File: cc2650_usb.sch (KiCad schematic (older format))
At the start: 29 parts, among them P1 CONN_01X07, P2 CONN_01X04, P3 CONN_01X02, U1 CC2650F128RHB, X1 24Mhz, Y1 32.768kHz

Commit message: Some layout work done
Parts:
- added P4: CONN_01X08, Pin_Headers:Pin_Header_Straight_1x08, symbol CONN_01X08
- ANT1: footprint (none) -> jyd:TI_DN007_2.4GHz
- C1, C10, C11, C12, C13, C14, C15, C16, C17, C2, C3, C4, C5, C6, C7, C8, C9, L1, L2, L3: footprint (none) -> Capacitors_SMD:C_0603
- P1: footprint (none) -> Pin_Headers:Pin_Header_Straight_1x07
- P2: footprint (none) -> Pin_Headers:Pin_Header_Straight_1x04
- P3: footprint (none) -> Pin_Headers:Pin_Header_Straight_1x02
- R1, R2: footprint (none) -> Resistors_SMD:R_0603
- U1: footprint (none) -> Housings_DFN_QFN:QFN-32-1EP_5x5mm_Pitch0.5mm
- X1: footprint (none) -> Crystals:crystal_FA238-TSX3225
- Y1: footprint (none) -> crystals_extra:XTAL3215
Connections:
- net labels added: DIO_10, DIO_11, DIO_12, DIO_13, DIO_14, DIO_7, DIO_8, DIO_9, RF_N, RF_P, X24M_N, X24M_P, X32K_Q1, X32K_Q2
- wire segments 97 -> 136
- no-connect marks 1 -> 4
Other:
- moved on the sheet: ANT1, C14, C15, C16, C17, L2, L3, R2

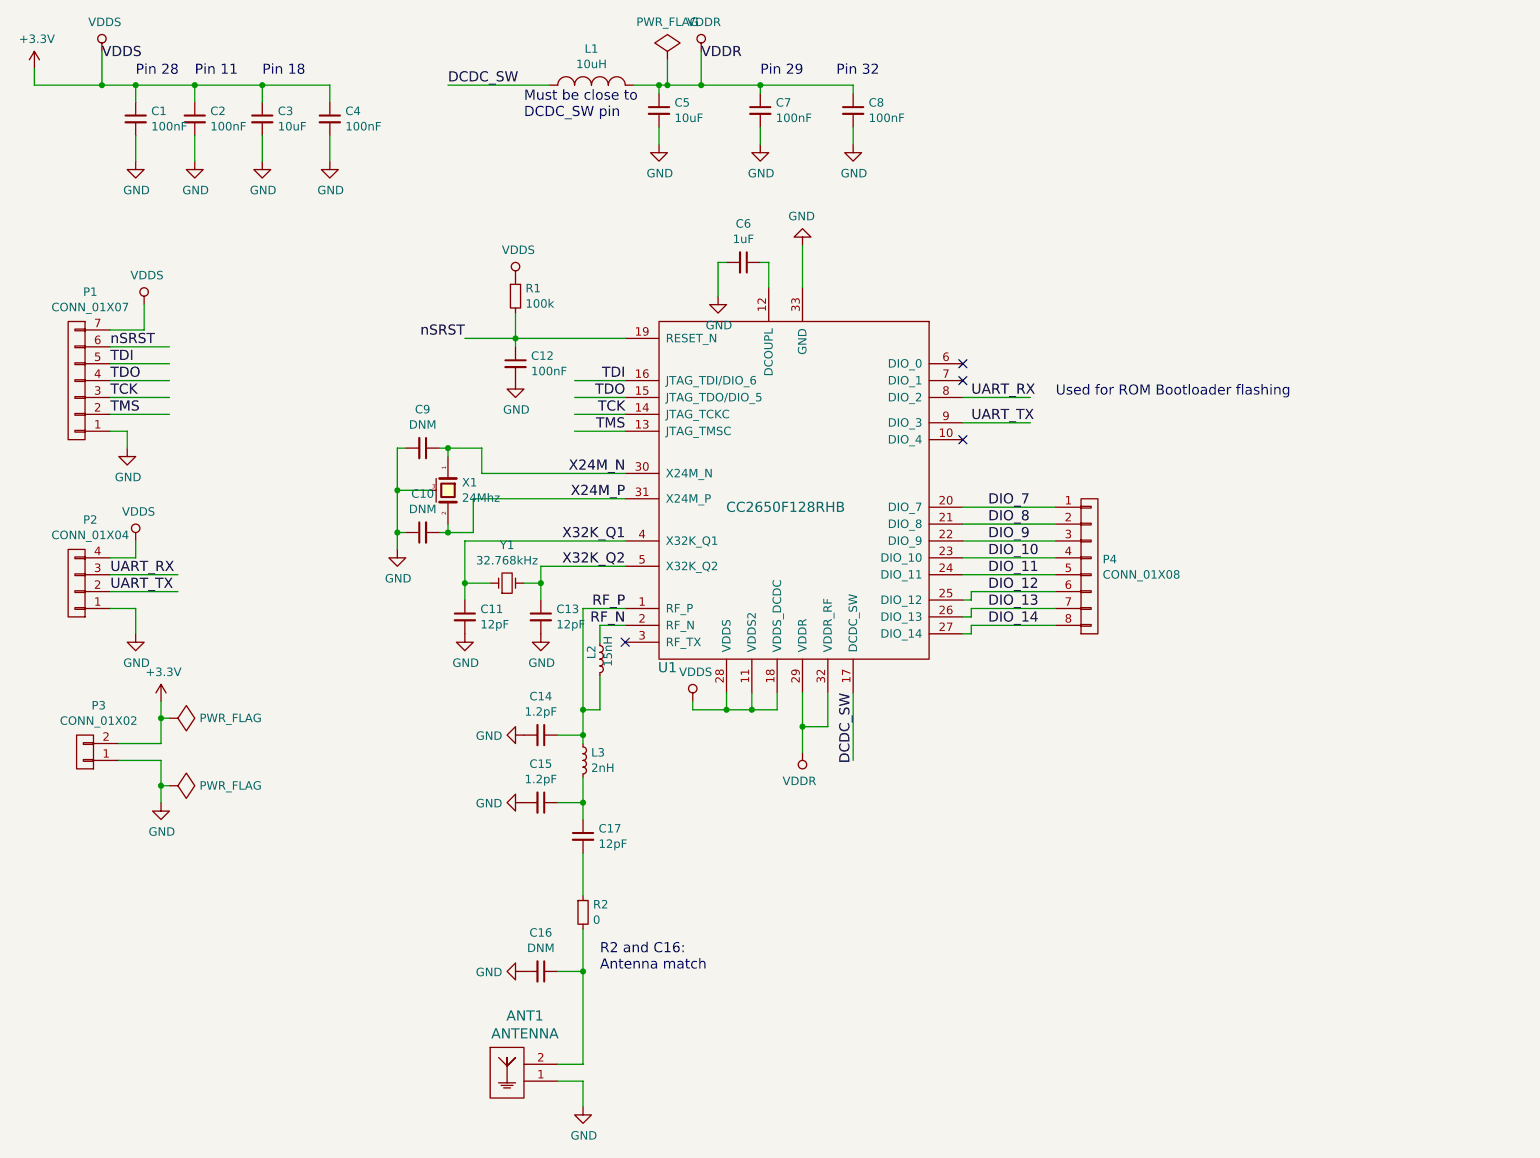
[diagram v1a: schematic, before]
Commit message: Add battery input, power led, usr button & usr led, transistor/diode for power switching
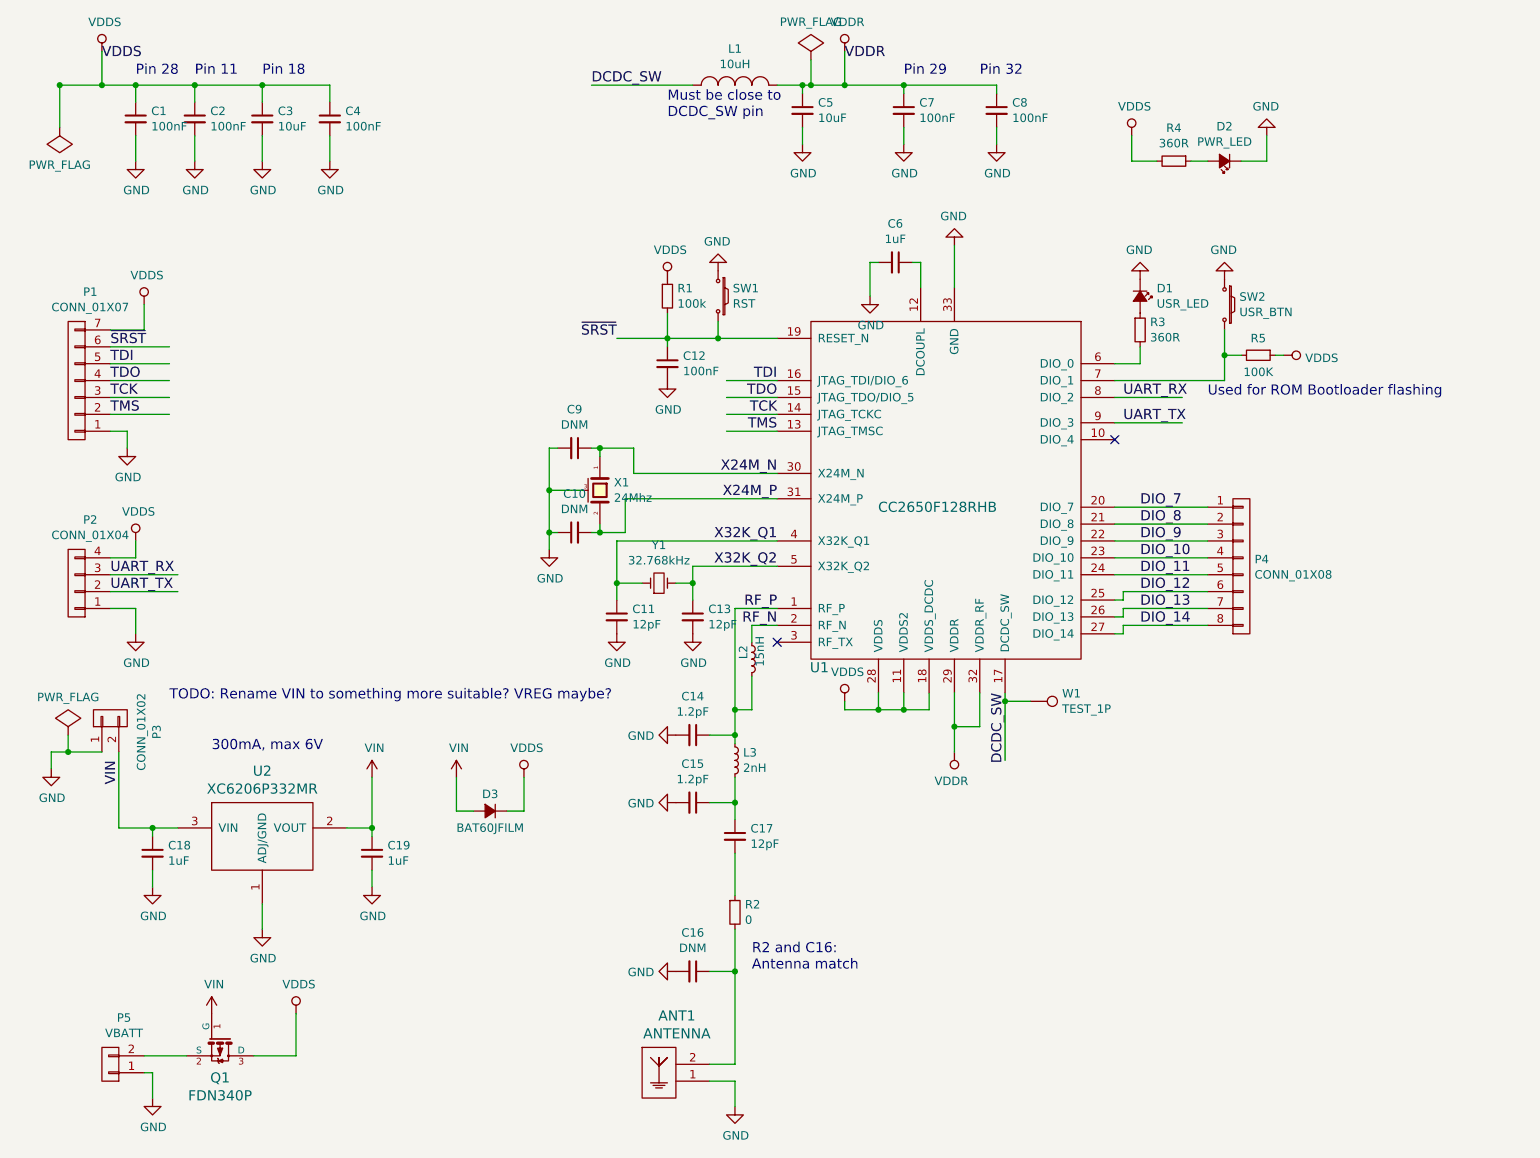
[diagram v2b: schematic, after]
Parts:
- added C18, C19: 1uF, Capacitors_SMD:C_0603, symbol C_Small
- added D1: USR_LED, LEDs:LED_0603, symbol Led_Small
- added D2: PWR_LED, LEDs:LED_0603, symbol Led_Small
- added D3: BAT60JFILM, Diodes_SMD:SOD-323, symbol D_Small
- added P5: VBATT, symbol CONN_01X02
- added Q1: FDN340P, TO_SOT_Packages_SMD:SOT-23, symbol FDN340P
- added R3, R4: 360R, Resistors_SMD:R_0603, symbol R_Small
- added R5: 100K, Resistors_SMD:R_0603, symbol R_Small
- added SW1: RST, symbol SW_PUSH_SMALL_H
- added SW2: USR_BTN, symbol SW_PUSH_SMALL_H
- added U2: XC6206P332MR, TO_SOT_Packages_SMD:SOT-23, symbol XC6206P332MR
- added W1: TEST_1P, Connect:PINTST, symbol TEST_1P
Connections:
- net labels added: VIN, ~SRST~
- net labels removed: +3.3V, nSRST
- wire segments 136 -> 138
- no-connect marks 4 -> 2
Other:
- note added: "300mA, max 6V"
- note added: "TODO: Rename VIN to something more suitable? VREG maybe?"
- moved on the sheet: ANT1, C10, C11, C12, C13, C14, C15, C16, C17, C5, C6, C7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

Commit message: More routing
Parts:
- P5: value VBATT -> VBAT; footprint (none) -> battery_extra:CR2032_SMD
- SW1, SW2: footprint (none) -> smallbutton:SmallButton
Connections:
- net labels added: USR_BTN, USR_LED, VBAT, VEXT
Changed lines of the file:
@@
 F 0 "SW1" V 4654 2287 50  0000 L CNN
 F 1 "RST" V 4745 2287 50  0000 L CNN
-F 2 "" H 4700 2400 50  0001 C CNN
+F 2 "smallbutton:SmallButton" H 4700 2400 50  0001 C CNN
 F 3 "" H 4700 2400 50  0000 C CNN
 	1    4700 2200
@@
 F 0 "SW2" V 7654 2338 50  0000 L CNN
 F 1 "USR_BTN" V 7745 2338 50  0000 L CNN
-F 2 "" H 7700 2450 50  0001 C CNN
+F 2 "smallbutton:SmallButton" H 7700 2450 50  0001 C CNN
 F 3 "" H 7700 2450 50  0000 C CNN
 	1    7700 2250
@@
 Wire Wire Line
 	1150 4900 1150 5350
-Text Label 1150 4950 3    60   ~ 0
-VIN
 $Comp
 L GND #PWR035
@@
 P 1100 6750
 F 0 "P5" H 1019 6475 50  0000 C CNN
-F 1 "VBATT" H 1019 6566 50  0000 C CNN
-F 2 "" H 1100 6750 50  0001 C CNN
+F 1 "VBAT" H 1019 6566 50  0000 C CNN
+F 2 "battery_extra:CR2032_SMD" H 1100 6750 50  0001 C CNN
 F 3 "" H 1100 6750 50  0000 C CNN
 	1    1100 6750
@@
 Text Notes 1450 4600 0    60   ~ 0
 TODO: Rename VIN to something more suitable? VREG maybe?
+Text Label 1150 5000 3    60   ~ 0
+VEXT
+Text Label 1350 6700 0    60   ~ 0
+VBAT
+Text Label 7050 2600 0    60   ~ 0
+USR_LED
+Text Label 7050 2700 0    60   ~ 0
+USR_BTN
 $EndSCHEMATC

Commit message: Routing almost done
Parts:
- removed R5: 100K, Resistors_SMD:R_0603, symbol R_Small
- removed SW2: USR_BTN, smallbutton:SmallButton, symbol SW_PUSH_SMALL_H
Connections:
- net labels added: DCOUPL
- net labels removed: USR_BTN
- wire segments 138 -> 134
- no-connect marks 2 -> 3
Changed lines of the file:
@@
 Connection ~ 6400 4600
-$Comp
-L SW_PUSH_SMALL_H SW2
-U 1 1 57C52995
-P 7700 2250
-F 0 "SW2" V 7654 2338 50  0000 L CNN
-F 1 "USR_BTN" V 7745 2338 50  0000 L CNN
-F 2 "smallbutton:SmallButton" H 7700 2450 50  0001 C CNN
-F 3 "" H 7700 2450 50  0000 C CNN
-	1    7700 2250
-	0    1    1    0
-$EndComp
-Wire Wire Line
-	7700 2700 7050 2700
-Wire Wire Line
-	7700 2400 7700 2700
-$Comp
-L GND #PWR032
-U 1 1 57C52FAD
-P 7700 2100
-F 0 "#PWR032" H 7700 1850 50  0001 C CNN
-F 1 "GND" H 7705 1927 50  0000 C CNN
-F 2 "" H 7700 2100 50  0000 C CNN
-F 3 "" H 7700 2100 50  0000 C CNN
-	1    7700 2100
-	-1   0    0    1
-$EndComp
-$Comp
-L R_Small R5
-U 1 1 57C53055
-P 7900 2550
-F 0 "R5" V 7800 2550 50  0000 C CNN
-F 1 "100K" V 8000 2550 50  0000 C CNN
-F 2 "Resistors_SMD:R_0603" H 7900 2550 50  0001 C CNN
-F 3 "" H 7900 2550 50  0000 C CNN
-	1    7900 2550
-	0    1    1    0
-$EndComp
-Wire Wire Line
-	7800 2550 7700 2550
-Connection ~ 7700 2550
-$Comp
-L VDDS #PWR033
-U 1 1 57C532AB
-P 8050 2550
-F 0 "#PWR033" H 8050 2400 50  0001 C CNN
-F 1 "VDDS" V 8067 2678 50  0000 L CNN
-F 2 "" H 8050 2550 50  0000 C CNN
-F 3 "" H 8050 2550 50  0000 C CNN
-	1    8050 2550
-	0    1    1    0
-$EndComp
-Wire Wire Line
-	8050 2550 8000 2550
 $Comp
 L XC6206P332MR U2
@@
 Text Label 7050 2600 0    60   ~ 0
 USR_LED
-Text Label 7050 2700 0    60   ~ 0
-USR_BTN
+Text Label 5900 2100 1    60   ~ 0
+DCOUPL
+NoConn ~ 7050 2700
 $EndSCHEMATC

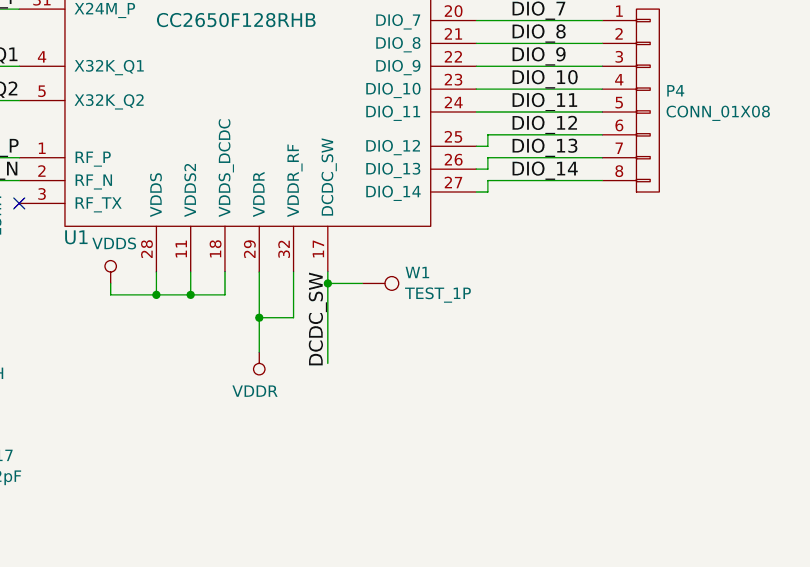
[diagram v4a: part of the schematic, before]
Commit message: More routing, remove useless TP
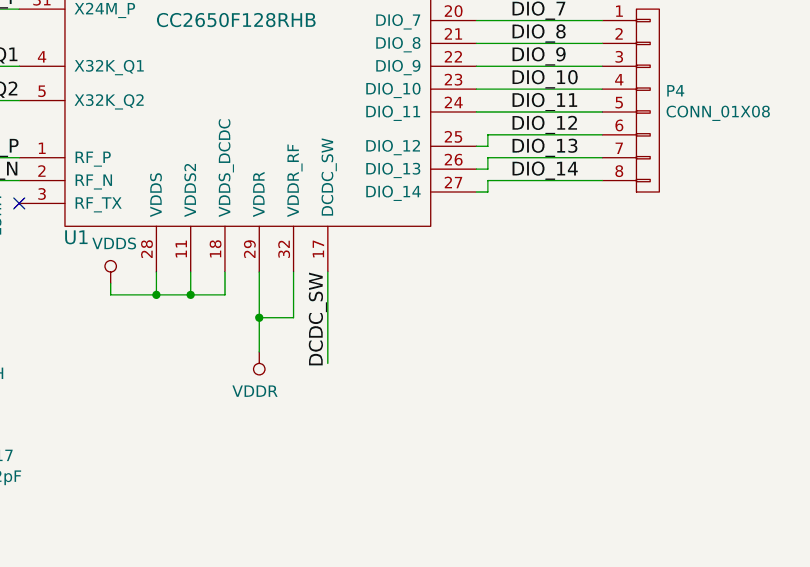
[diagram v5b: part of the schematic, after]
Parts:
- removed W1: TEST_1P, Connect:PINTST, symbol TEST_1P
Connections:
- wire segments 134 -> 133
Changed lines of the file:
@@
 	-1   0    0    1
 $EndComp
-$Comp
-L TEST_1P W1
-U 1 1 57C4EACF
-P 6550 4600
-F 0 "W1" V 6504 4788 50  0000 L CNN
-F 1 "TEST_1P" V 6595 4788 50  0000 L CNN
-F 2 "Connect:PINTST" H 6750 4600 50  0001 C CNN
-F 3 "" H 6750 4600 50  0000 C CNN
-	1    6550 4600
-	0    1    1    0
-$EndComp
 Wire Wire Line
 	7050 2800 7450 2800
@@
 Wire Wire Line
 	7600 1400 7500 1400
-Wire Wire Line
-	6400 4600 6550 4600
-Connection ~ 6400 4600
 $Comp
 L XC6206P332MR U2
